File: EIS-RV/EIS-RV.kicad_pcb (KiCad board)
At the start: 2 copper layers, 70 x 40 mm, 70 parts, among them IC1 MCP73831/OT, IC2 MCP73831/OT, Q1 2.5A/30V/105mΩ

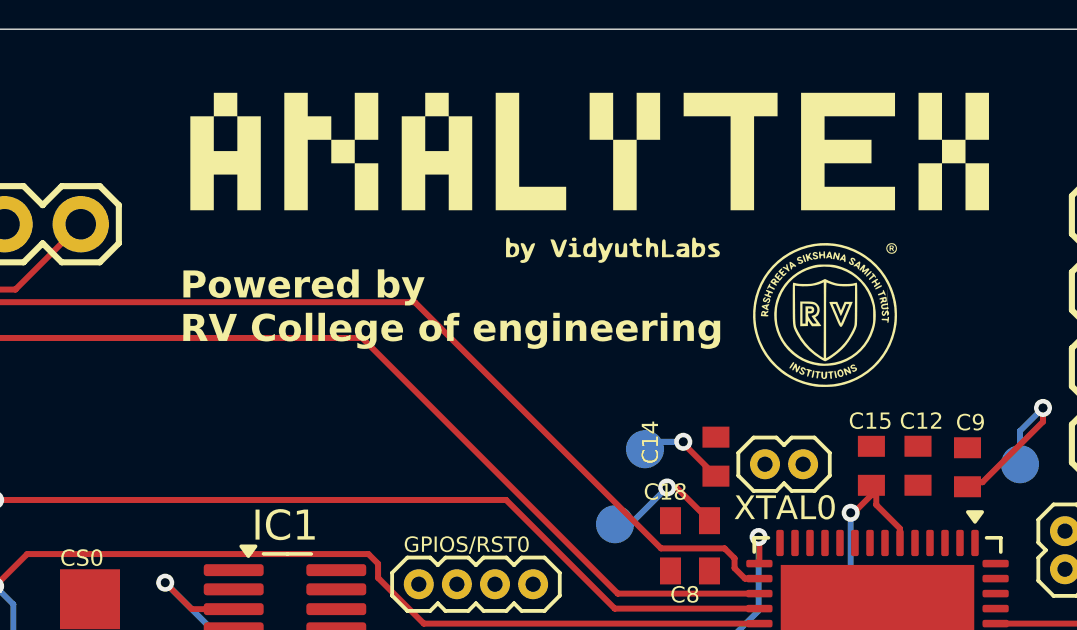
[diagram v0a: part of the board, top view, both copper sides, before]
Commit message: Add deployment configuration and comprehensive tests
- Add Render.com deployment (render.yaml)
- Add Docker deployment (Dockerfile, docker-compose.yml)
- Add CI/CD pipeline (.github/workflows/ci.yml)
- Add comprehensive test suites (195 tests, all passing)
- Add deployment guides and researcher documentation
- Ready for free cloud deployment
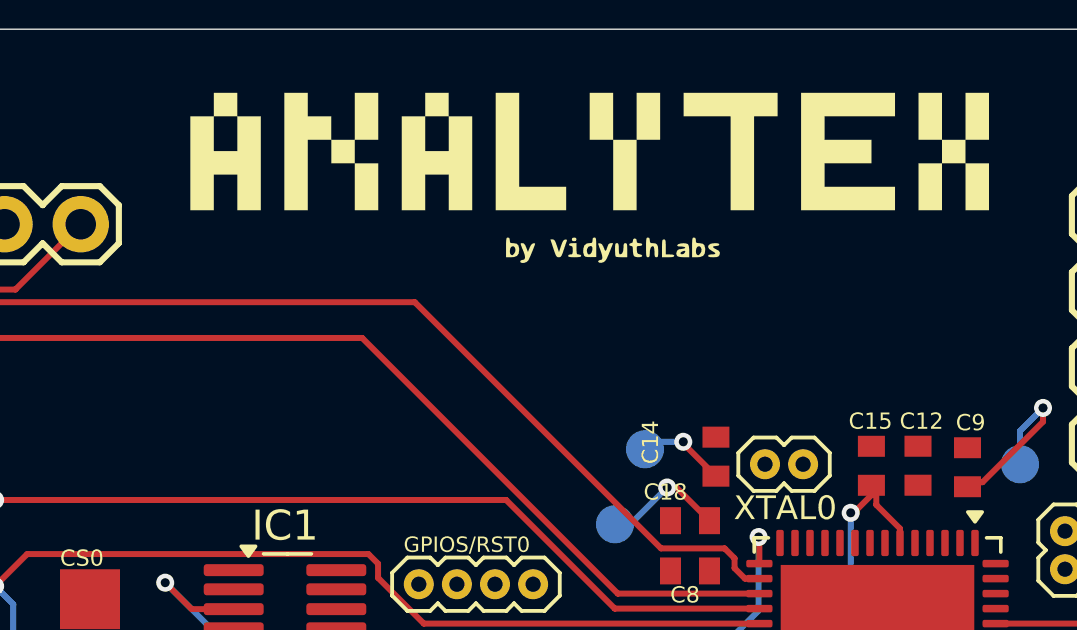
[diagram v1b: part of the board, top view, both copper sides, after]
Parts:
- removed RVCE: LOGO, LOGO
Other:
- board text removed: "Powered by RV College of engineering"
